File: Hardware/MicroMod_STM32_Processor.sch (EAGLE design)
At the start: 37 parts, among them J1 MICROMOD-2222, Q1 MOSFET_PCH-DMG2305UX-7, U1 STM32F405RGT6, U3 W25QXX128MBIT-6X5, Y1 12MHz, Y2 32.768kHz

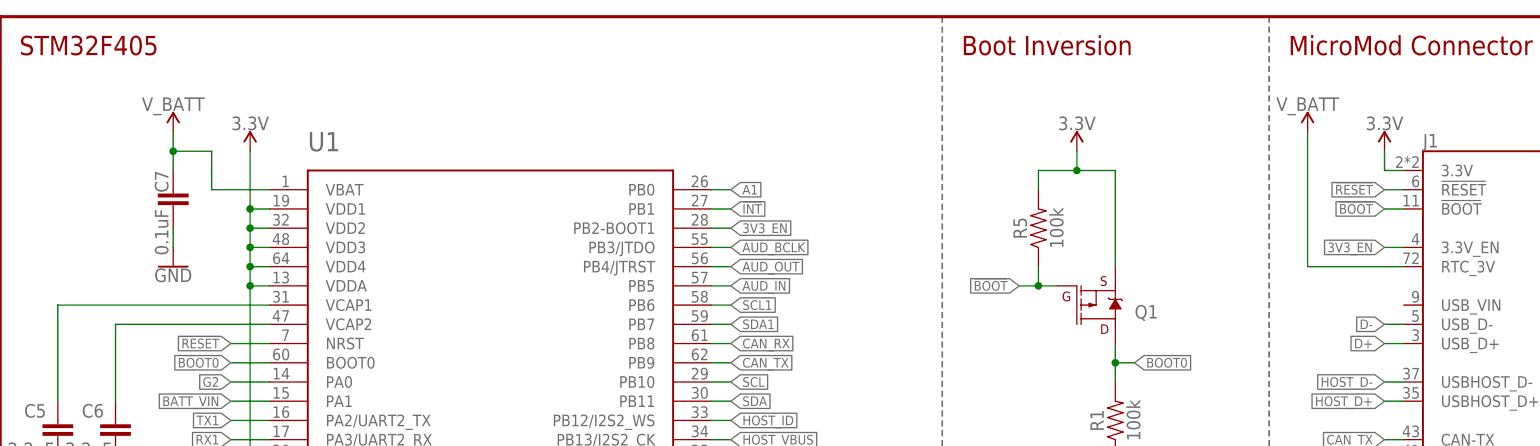
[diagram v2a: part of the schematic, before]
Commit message: V10 design review changes
Removed battery and 3.3V_EN connections to MicroMod
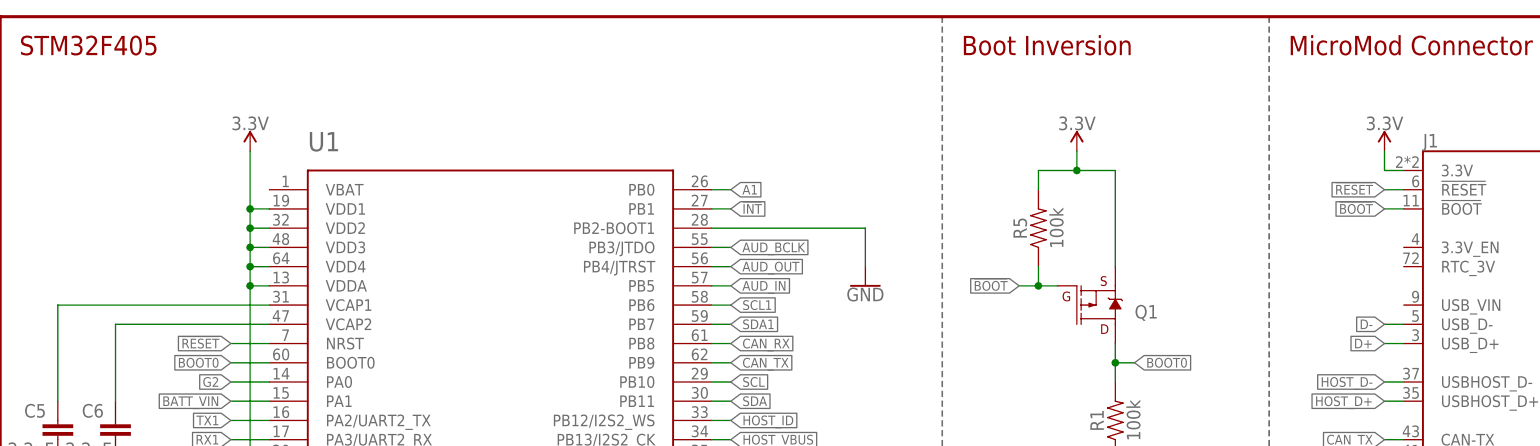
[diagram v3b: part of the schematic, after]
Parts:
- removed C7: 0.1uF, SparkFun-Capacitors:0.1UF-0402T-10V-10%-X7R
- C15: device SparkFun-Capacitors:0.1UF-0402T-6.3V-10%-X7R -> SparkFun-Capacitors:0.1UF-0402-10V-10%-X7R
- C8: device SparkFun-Capacitors:0.1UF-0402T-10V-10%-X7R -> SparkFun-Capacitors:0.1UF-0402-10V-10%-X7R
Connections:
- removed net 3V3_EN: J1.3.3V_EN, U1.PB2-BOOT1
- removed net V_BATT: C7.1, J1.RTC_3V, U1.VBAT
- net GND: now also U1.PB2-BOOT1; no longer C7.2
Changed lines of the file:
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@@
 <part name="GND20" library="SparkFun-PowerSymbols" deviceset="GND" device=""/>
 <part name="SUPPLY2" library="SparkFun-PowerSymbols" deviceset="3.3V" device=""/>
-<part name="C7" library="SparkFun-Capacitors" deviceset="0.1UF" device="-0402T-10V-10%-X7R" value="0.1uF"/>
-<part name="C8" library="SparkFun-Capacitors" deviceset="0.1UF" device="-0402T-10V-10%-X7R" value="0.1uF">
+<part name="C8" library="SparkFun-Capacitors" deviceset="0.1UF" device="-0402-10V-10%-X7R" value="0.1uF">
 <attribute name="SPICEPREFIX" value="C"/>
 </part>
@@
 <attribute name="SPICEPREFIX" value="C"/>
 </part>
-<part name="GND8" library="SparkFun-PowerSymbols" deviceset="GND" device=""/>
 <part name="GND9" library="SparkFun-PowerSymbols" deviceset="GND" device="">
 <attribute name="SPICEPREFIX" value="G"/>
@@
 <attribute name="SPICEPREFIX" value="G"/>
 </part>
-<part name="SUPPLY7" library="SparkFun-PowerSymbols" deviceset="V_BATT" device=""/>
 <part name="SUPPLY25" library="SparkFun-PowerSymbols" deviceset="3.3V" device=""/>
 <part name="GND1" library="SparkFun-PowerSymbols" deviceset="GND" device=""/>
@@
 <part name="SUPPLY1" library="SparkFun-PowerSymbols" deviceset="3.3V" device=""/>
 <part name="SUPPLY3" library="SparkFun-PowerSymbols" deviceset="3.3V" device=""/>
-<part name="SUPPLY4" library="SparkFun-PowerSymbols" deviceset="V_BATT" device=""/>
 <part name="D5" library="SparkFun-LED" deviceset="LED-BLUE" device="0603" value="BLUE"/>
 <part name="R12" library="SparkFun-Resistors" deviceset="1KOHM" device="-0402T-1/16W-1%" value="1k"/>
@@
 <part name="R3" library="SparkFun-Resistors" deviceset="22OHM" device="-0402T-1/16W-1%" value="22"/>
 <part name="R4" library="SparkFun-Resistors" deviceset="5.1KOHM" device="-0402T-1/16W-1%" value="5.1k"/>
-<part name="C15" library="SparkFun-Capacitors" deviceset="0.1UF" device="-0402T-6.3V-10%-X7R" value="0.1uF"/>
+<part name="C15" library="SparkFun-Capacitors" deviceset="0.1UF" device="-0402-10V-10%-X7R" value="0.1uF"/>
 <part name="SUPPLY5" library="SparkFun-PowerSymbols" deviceset="3.3V" device=""/>
 <part name="GND16" library="SparkFun-PowerSymbols" deviceset="GND" device=""/>
@@
 <part name="LOGO2" library="SparkFun-Aesthetics" deviceset="OSHW-LOGO" device="S"/>
 <part name="LOGO3" library="SparkFun-Aesthetics" deviceset="SFE_LOGO_NAME_FLAME" device=".1_INCH"/>
+<part name="GND8" library="SparkFun-PowerSymbols" deviceset="GND" device=""/>
 </parts>
 <sheets>
@@
 <attribute name="VALUE" x="45.72" y="61.214" size="1.778" layer="96" font="vector" align="bottom-center"/>
 </instance>
-<instance part="C7" gate="G$1" x="22.86" y="160.02" smashed="yes" rot="MR0">
-<attribute name="NAME" x="22.225" y="165.1" size="1.778" layer="95" font="vector" rot="MR270"/>
-<attribute name="VALUE" x="22.225" y="160.02" size="1.778" layer="96" font="vector" rot="MR270"/>
-</instance>
 <instance part="C8" gate="G$1" x="10.16" y="48.26" smashed="yes" rot="MR0">
 <attribute name="NAME" x="9.525" y="54.102" size="1.778" layer="95" font="vector" rot="MR270"/>
@@
 <attribute name="VALUE" x="24.511" y="48.26" size="1.778" layer="96" font="vector" rot="MR270"/>
 </instance>
-<instance part="GND8" gate="1" x="22.86" y="152.4" smashed="yes">
-<attribute name="VALUE" x="22.86" y="152.146" size="1.778" layer="96" font="vector" align="top-center"/>
-</instance>
 <instance part="GND9" gate="1" x="25.4" y="40.64" smashed="yes" rot="MR0">
 <attribute name="VALUE" x="25.4" y="40.386" size="1.778" layer="96" font="vector" rot="MR0" align="top-center"/>
@@
 <attribute name="VALUE" x="10.16" y="40.386" size="1.778" layer="96" font="vector" rot="MR0" align="top-center"/>
 </instance>
-<instance part="SUPPLY7" gate="G$1" x="22.86" y="170.18" smashed="yes">
-<attribute name="VALUE" x="22.86" y="172.974" size="1.778" layer="96" font="vector" align="bottom-center"/>
-</instance>
 <instance part="SUPPLY25" gate="G$1" x="10.16" y="58.42" smashed="yes" rot="MR0">
 <attribute name="VALUE" x="10.16" y="61.214" size="1.778" layer="96" font="vector" rot="MR0" align="bottom-center"/>
@@
 <instance part="SUPPLY3" gate="G$1" x="182.88" y="167.64" smashed="yes">
 <attribute name="VALUE" x="182.88" y="170.434" size="1.778" layer="96" font="vector" align="bottom-center"/>
-</instance>
-<instance part="SUPPLY4" gate="G$1" x="172.72" y="170.18" smashed="yes">
-<attribute name="VALUE" x="172.72" y="172.974" size="1.778" layer="96" font="vector" align="bottom-center"/>
 </instance>
 <instance part="D5" gate="G$1" x="25.4" y="12.7" smashed="yes" rot="R90">
@@
 <instance part="LOGO2" gate="G$1" x="233.68" y="48.26" smashed="yes"/>
 <instance part="LOGO3" gate="G$1" x="162.56" y="35.56" smashed="yes"/>
+<instance part="GND8" gate="1" x="114.3" y="149.86" smashed="yes">
+<attribute name="VALUE" x="114.3" y="149.606" size="1.778" layer="96" font="vector" align="top-center"/>
+</instance>
 </instances>
 <busses>
@@
 </segment>
 </net>
-<net name="3V3_EN" class="0">
-<segment>
-<pinref part="J1" gate="J1" pin="3.3V_EN"/>
-<wire x1="185.42" y1="154.94" x2="182.88" y2="154.94" width="0.1524" layer="91"/>
-<label x="182.88" y="154.94" size="1.27" layer="95" font="vector" rot="R180" xref="yes"/>
-</segment>
-<segment>
-<pinref part="U1" gate="G$1" pin="PB2-BOOT1"/>
-<wire x1="93.98" y1="157.48" x2="96.52" y2="157.48" width="0.1524" layer="91"/>
-<label x="96.52" y="157.48" size="1.27" layer="95" font="vector" xref="yes"/>
-</segment>
-</net>
 <net name="G4" class="0">
 <segment>
@@
 <wire x1="53.34" y1="45.72" x2="53.34" y2="43.18" width="0.1524" layer="91"/>
 <pinref part="GND20" gate="1" pin="GND"/>
-</segment>
-<segment>
-<pinref part="C7" gate="G$1" pin="2"/>
-<wire x1="22.86" y1="157.48" x2="22.86" y2="154.94" width="0.1524" layer="91"/>
-<pinref part="GND8" gate="1" pin="GND"/>
 </segment>
 <segment>
@@
 <wire x1="144.78" y1="71.12" x2="144.78" y2="68.58" width="0.1524" layer="91"/>
 <pinref part="GND16" gate="1" pin="GND"/>
+</segment>
+<segment>
+<pinref part="U1" gate="G$1" pin="PB2-BOOT1"/>
+<wire x1="93.98" y1="157.48" x2="114.3" y2="157.48" width="0.1524" layer="91"/>
+<wire x1="114.3" y1="157.48" x2="114.3" y2="152.4" width="0.1524" layer="91"/>
+<pinref part="GND8" gate="1" pin="GND"/>
 </segment>
 </net>
@@
 </segment>
 </net>
-<net name="V_BATT" class="0">
-<segment>
-<wire x1="27.94" y1="167.64" x2="22.86" y2="167.64" width="0.1524" layer="91"/>
-<pinref part="C7" gate="G$1" pin="1"/>
-<wire x1="22.86" y1="165.1" x2="22.86" y2="167.64" width="0.1524" layer="91"/>
-<pinref part="SUPPLY7" gate="G$1" pin="V_BATT"/>
-<wire x1="22.86" y1="170.18" x2="22.86" y2="167.64" width="0.1524" layer="91"/>
-<junction x="22.86" y="167.64"/>
-<pinref part="U1" gate="G$1" pin="VBAT"/>
-<wire x1="35.56" y1="162.56" x2="27.94" y2="162.56" width="0.1524" layer="91"/>
-<wire x1="27.94" y1="162.56" x2="27.94" y2="167.64" width="0.1524" layer="91"/>
-</segment>
-<segment>
-<pinref part="J1" gate="J1" pin="RTC_3V"/>
-<pinref part="SUPPLY4" gate="G$1" pin="V_BATT"/>
-<wire x1="185.42" y1="152.4" x2="172.72" y2="152.4" width="0.1524" layer="91"/>
-<wire x1="172.72" y1="152.4" x2="172.72" y2="170.18" width="0.1524" layer="91"/>
-</segment>
-</net>

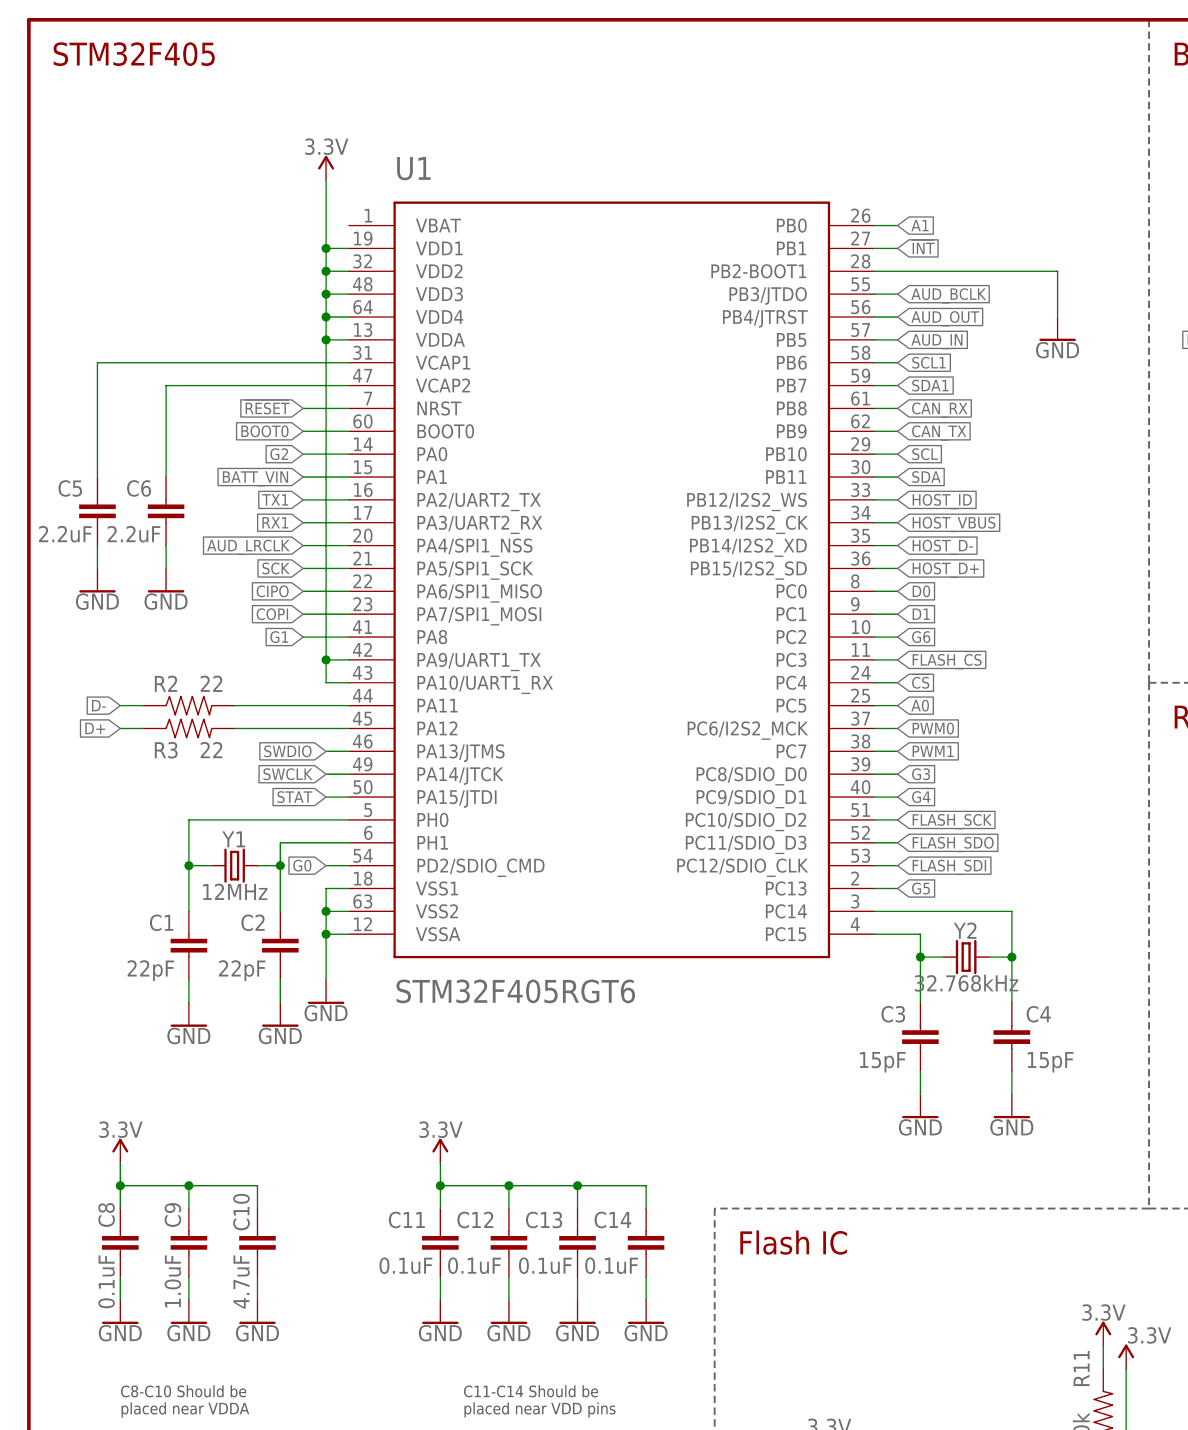
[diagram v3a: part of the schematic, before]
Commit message: Double-check changes
- Added VDD range
- Updated 0.1uF cap footprints from 0402 to 0402_TIGHT
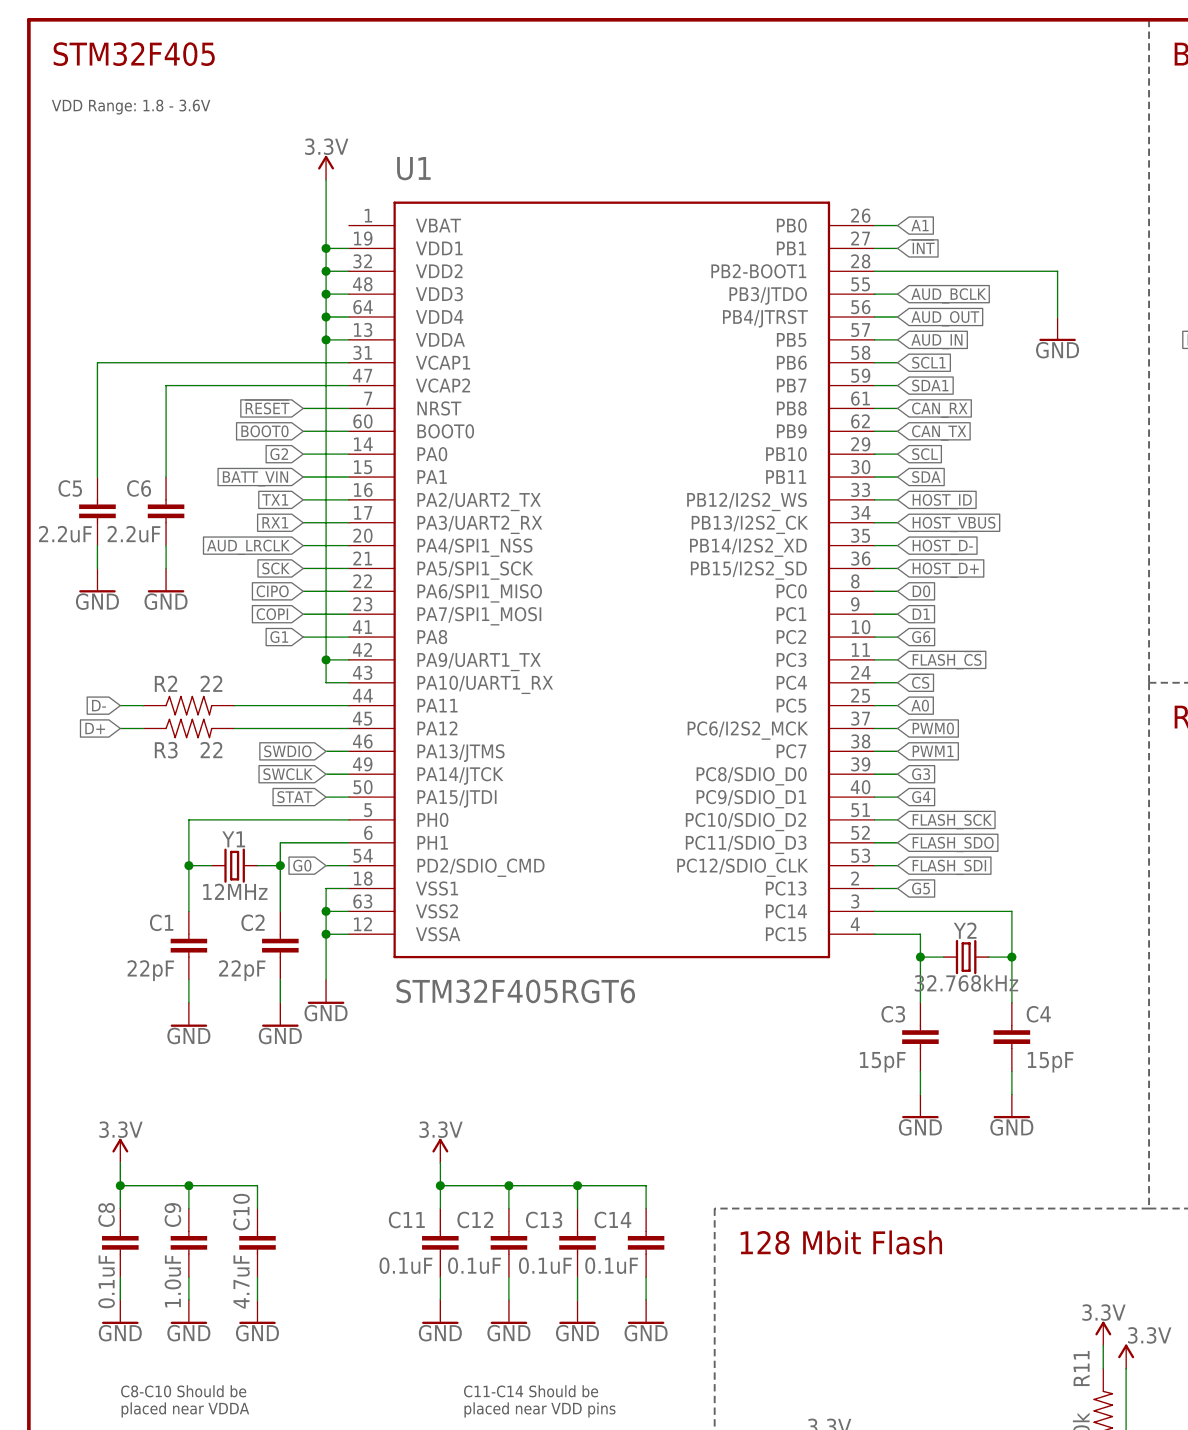
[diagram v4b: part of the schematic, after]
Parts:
- C15, C8: device SparkFun-Capacitors:0.1UF-0402-10V-10%-X7R -> SparkFun-Capacitors:0.1UF-0402T-10V-10%-X7R
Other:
- note added: "128 Mbit Flash"
- note added: "VDD Range: 1.8 - 3.6V"
- note removed: "Flash IC"
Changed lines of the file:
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@@
 <part name="GND20" library="SparkFun-PowerSymbols" deviceset="GND" device=""/>
 <part name="SUPPLY2" library="SparkFun-PowerSymbols" deviceset="3.3V" device=""/>
-<part name="C8" library="SparkFun-Capacitors" deviceset="0.1UF" device="-0402-10V-10%-X7R" value="0.1uF">
+<part name="C8" library="SparkFun-Capacitors" deviceset="0.1UF" device="-0402T-10V-10%-X7R" value="0.1uF">
 <attribute name="SPICEPREFIX" value="C"/>
 </part>
@@
 <part name="R3" library="SparkFun-Resistors" deviceset="22OHM" device="-0402T-1/16W-1%" value="22"/>
 <part name="R4" library="SparkFun-Resistors" deviceset="5.1KOHM" device="-0402T-1/16W-1%" value="5.1k"/>
-<part name="C15" library="SparkFun-Capacitors" deviceset="0.1UF" device="-0402-10V-10%-X7R" value="0.1uF"/>
+<part name="C15" library="SparkFun-Capacitors" deviceset="0.1UF" device="-0402T-10V-10%-X7R" value="0.1uF"/>
 <part name="SUPPLY5" library="SparkFun-PowerSymbols" deviceset="3.3V" device=""/>
 <part name="GND16" library="SparkFun-PowerSymbols" deviceset="GND" device=""/>
@@
 <sheet>
 <plain>
-<text x="78.74" y="48.26" size="2.54" layer="94" font="vector" ratio="15">Flash IC</text>
+<text x="78.74" y="48.26" size="2.54" layer="94" font="vector" ratio="15">128 Mbit Flash</text>
 <text x="2.54" y="22.86" size="2.54" layer="94" font="vector" ratio="15">Status LED</text>
 <wire x1="124.46" y1="185.42" x2="124.46" y2="111.76" width="0.2032" layer="97" style="shortdash"/>
@@
 <text x="165.1" y="11.684" size="2.54" layer="94" font="vector" ratio="15">Alex Wende</text>
 <wire x1="45.72" y1="27.94" x2="45.72" y2="0" width="0.2032" layer="97" style="shortdash"/>
+<text x="2.54" y="175.26" size="1.27" layer="97">VDD Range: 1.8 - 3.6V</text>
 </plain>
 <instances>

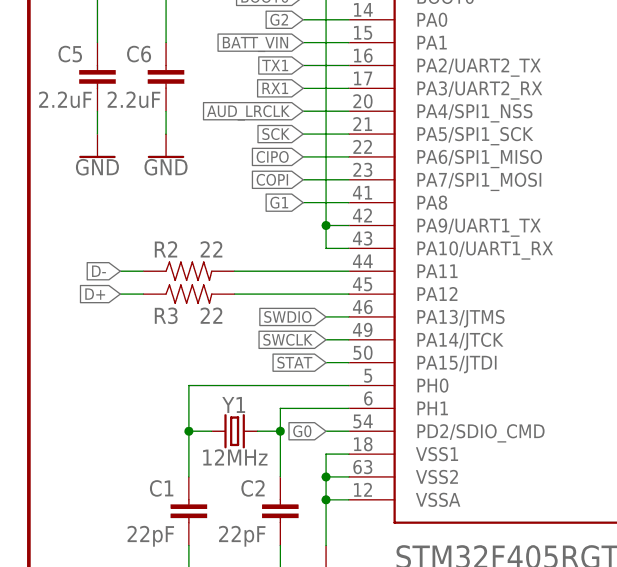
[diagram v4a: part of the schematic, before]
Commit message: Updated BOM
Replaced 22 ohm resistors with 0 ohm
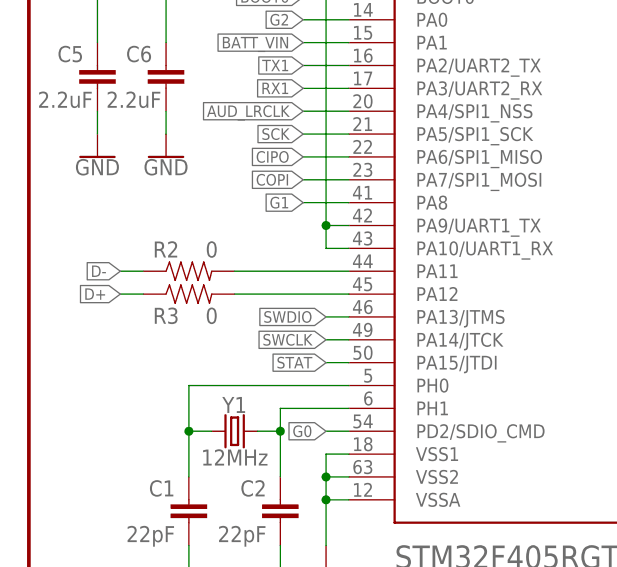
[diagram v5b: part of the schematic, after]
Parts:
- R2, R3: value 22 -> 0; device SparkFun-Resistors:22OHM-0402T-1/16W-1% -> SparkFun-Resistors:0OHM-0402T-1/10W
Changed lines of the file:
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@@
 <?xml version="1.0" encoding="utf-8"?>
 <!DOCTYPE eagle SYSTEM "eagle.dtd">
-<eagle version="9.6.2">
+<eagle version="9.5.2">
 <drawing>
 <settings>
@@
 <part name="R12" library="SparkFun-Resistors" deviceset="1KOHM" device="-0402T-1/16W-1%" value="1k"/>
 <part name="GND35" library="SparkFun-PowerSymbols" deviceset="GND" device=""/>
-<part name="R2" library="SparkFun-Resistors" deviceset="22OHM" device="-0402T-1/16W-1%" value="22"/>
-<part name="R3" library="SparkFun-Resistors" deviceset="22OHM" device="-0402T-1/16W-1%" value="22"/>
+<part name="R2" library="SparkFun-Resistors" deviceset="0OHM" device="-0402T-1/10W" value="0"/>
+<part name="R3" library="SparkFun-Resistors" deviceset="0OHM" device="-0402T-1/10W" value="0"/>
 <part name="R4" library="SparkFun-Resistors" deviceset="5.1KOHM" device="-0402T-1/16W-1%" value="5.1k"/>
 <part name="C15" library="SparkFun-Capacitors" deviceset="0.1UF" device="-0402T-10V-10%-X7R" value="0.1uF"/>
